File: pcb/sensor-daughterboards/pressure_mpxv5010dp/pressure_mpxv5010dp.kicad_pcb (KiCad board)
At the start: 2 copper layers, 42 x 25 mm, 12 parts, among them J1 Main board connections (botto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, J2 Main board connections (botto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, U1 MPXV5004DP

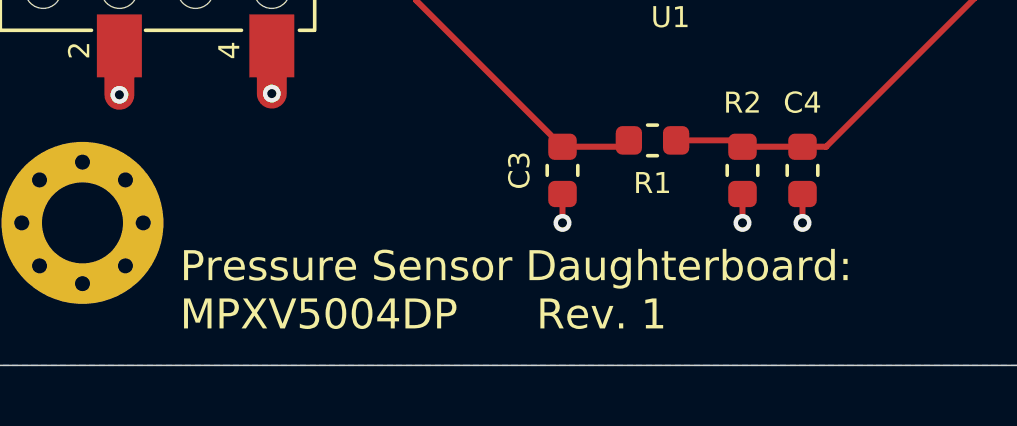
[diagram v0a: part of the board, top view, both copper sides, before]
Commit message: Pressure sensor daughterboards
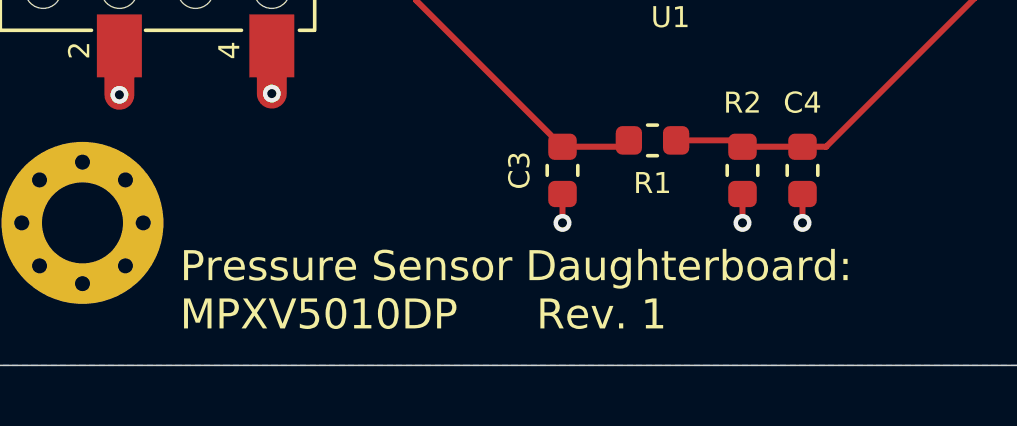
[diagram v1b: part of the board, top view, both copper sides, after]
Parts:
- U1: value MPXV5004DP -> MPXV5010DP; footprint RespiraWorks:NXP_MPXV5004DP -> RespiraWorks:NXP_MPXV5010DP
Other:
- board text added: "Pressure Sensor Daughterboard: MPXV5010DP Rev. 1"
- board text removed: "Pressure Sensor Daughterboard: MPXV5004DP Rev. 1"
